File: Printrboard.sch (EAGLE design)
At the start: 121 parts, among them J1 MICROSD, J2 USB-MICROB, J3 ATX, Q1 RFP30N06LE, Q2 RFP30N06LE, Q3 RFP30N06LE, U1 LM2841, U2 A4982, U3 A4982, U4 A4982, U5 A4982, U6 AT90USB1286, U7 AP7313, U8 TXB0104, X1 16MHz

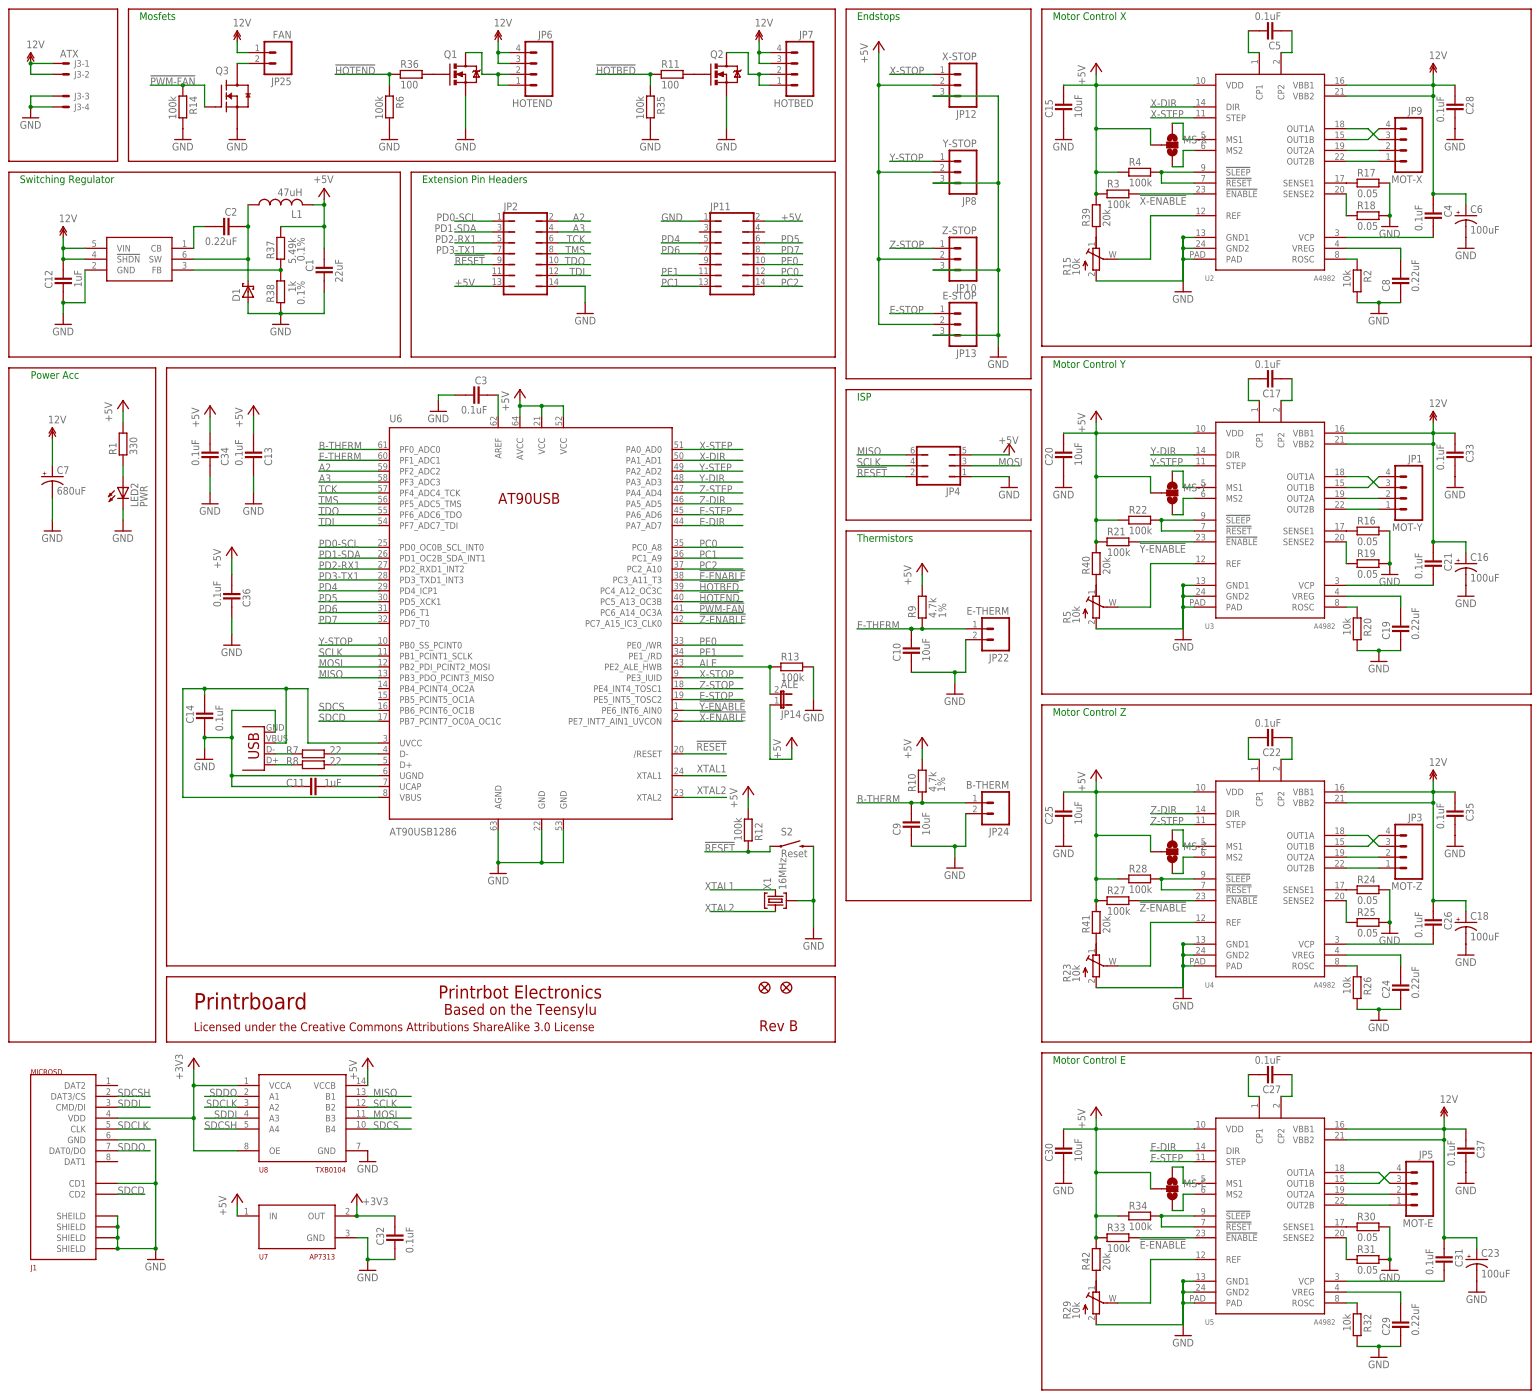
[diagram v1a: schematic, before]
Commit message: Change some caps around, add a solder jumper for USB sourced 5V, and modify silkscreen for production
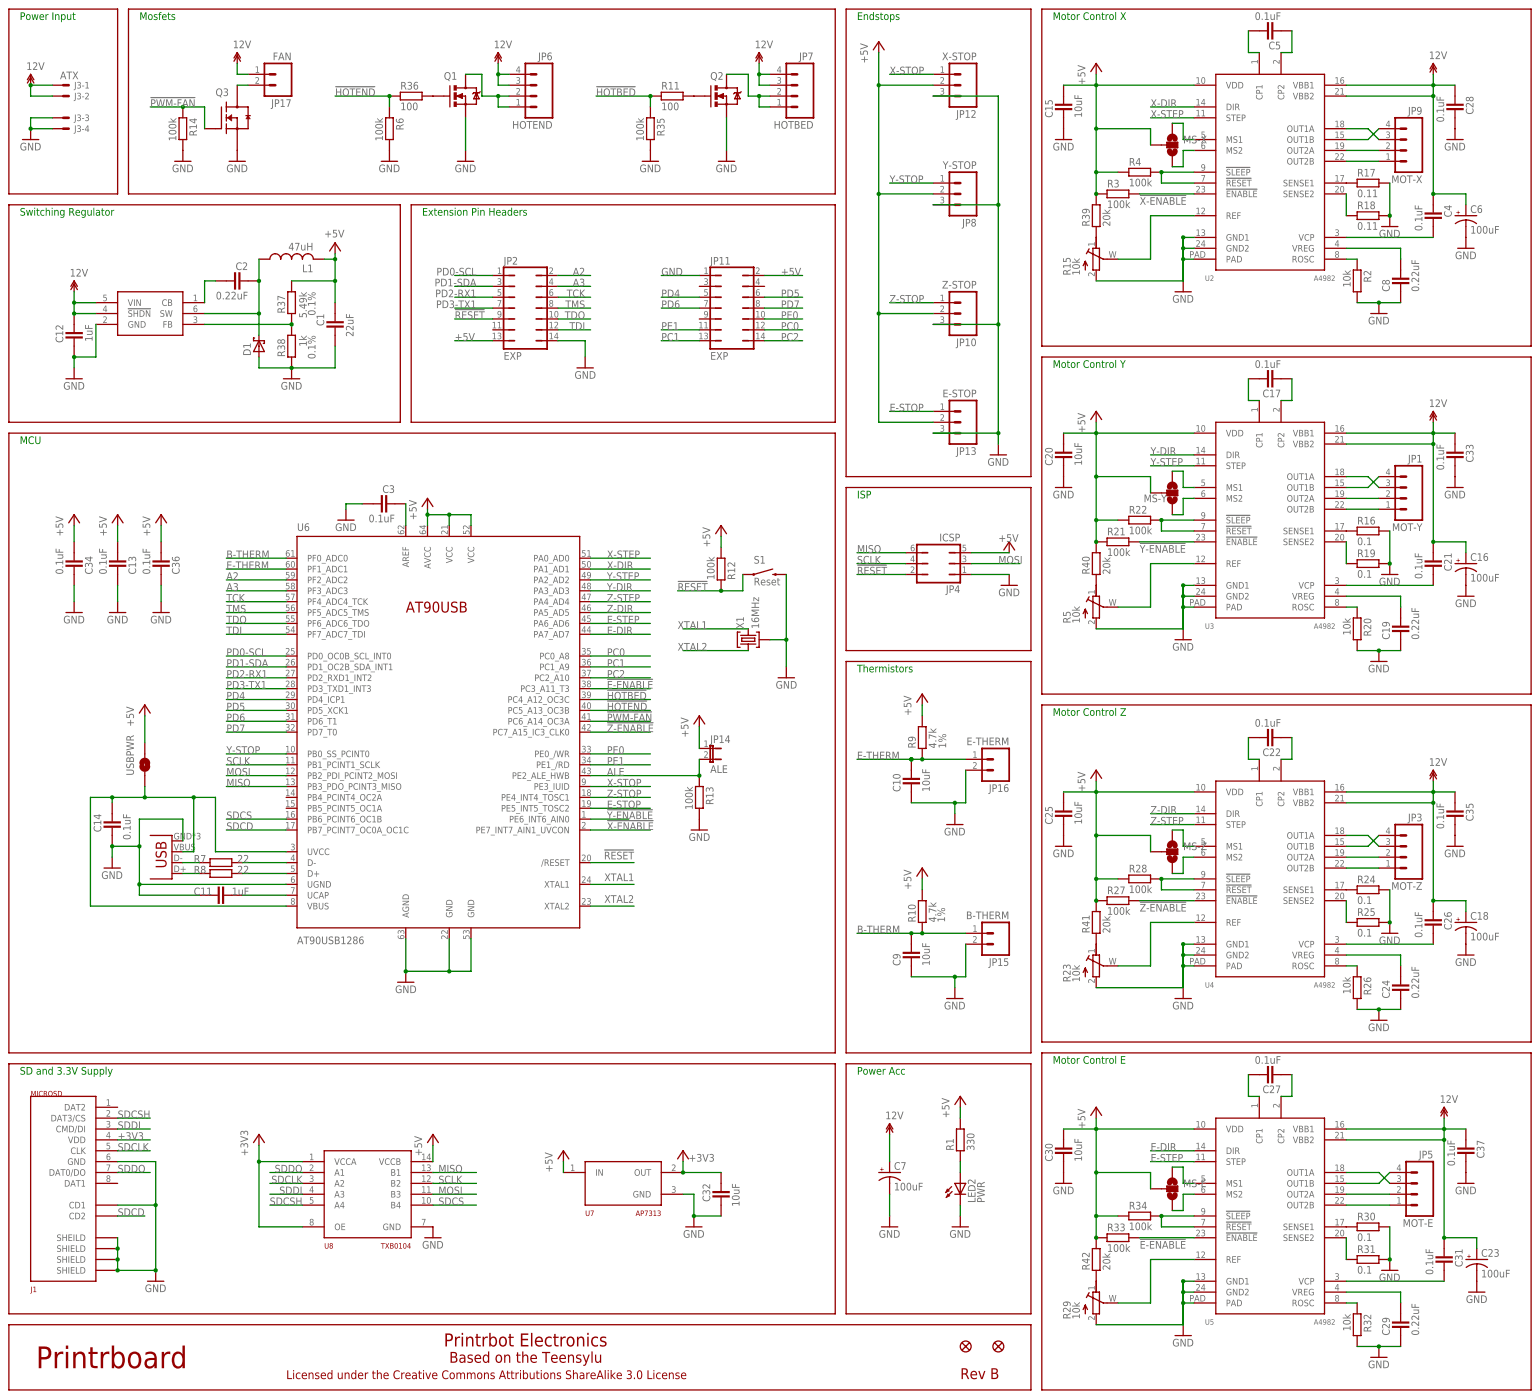
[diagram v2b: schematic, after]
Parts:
- removed J2: USB-MICROB, SparkFun:USB-MICROB
- removed JP22: E-THERM, SparkFun:M02PTH
- removed JP24: B-THERM, SparkFun:M02PTH
- removed JP25: FAN, SparkFun:M02PTH
- removed S2: Reset, SparkFun:SWITCH-MOMENTARY-2
- added JP15: B-THERM, SparkFun:M02PTH
- added JP16: E-THERM, SparkFun:M02PTH
- added JP17: FAN, SparkFun:M02PTH
- added S1: Reset, printrbot:SWITCH-MOMENTARY-2
- added USBPWR: SOLDERJUMPERNO, SparkFun:SOLDERJUMPERNO
- added X2: USB-MICROB, printrbot:USB-MICROB
- C32: value 0.1uF -> 10uF
- C7: value 680uF -> 100uF; device rcl:CPOL-USF -> rcl:CPOL-USD
- JP11, JP2: value (none) -> EXP
- JP4: value (none) -> ICSP
- R16, R19, R24, R25, R30, R31: value 0.05 -> 0.1
- R17, R18: value 0.05 -> 0.11
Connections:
- net !RESET: now also S1.1; no longer S2.1
- net +5V: now also USBPWR.2
- net 12V: now also JP17.1; no longer JP25.1
- net B-THERM: now also JP15.1; no longer JP24.1
- net E-THERM: now also JP16.1; no longer JP22.1
- net GND: now also JP15.2, JP16.2, S1.2, X2.GND; no longer J2.GND, JP22.2, JP24.2, S2.2
- net N$2: now also X2.D-; no longer J2.D-
- net N$5: now also X2.D+; no longer J2.D+
- net N$6: now also JP17.2; no longer JP25.2
- net VBUS: now also USBPWR.1, X2.VBUS; no longer J2.VBUS
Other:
- note added: "MCU"
- note added: "Power Input"
- note added: "SD and 3.3V Supply"
- moved on the sheet: C1, C10, C11, C12, C13, C14, C2, C3, C32, C34, C36, C7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

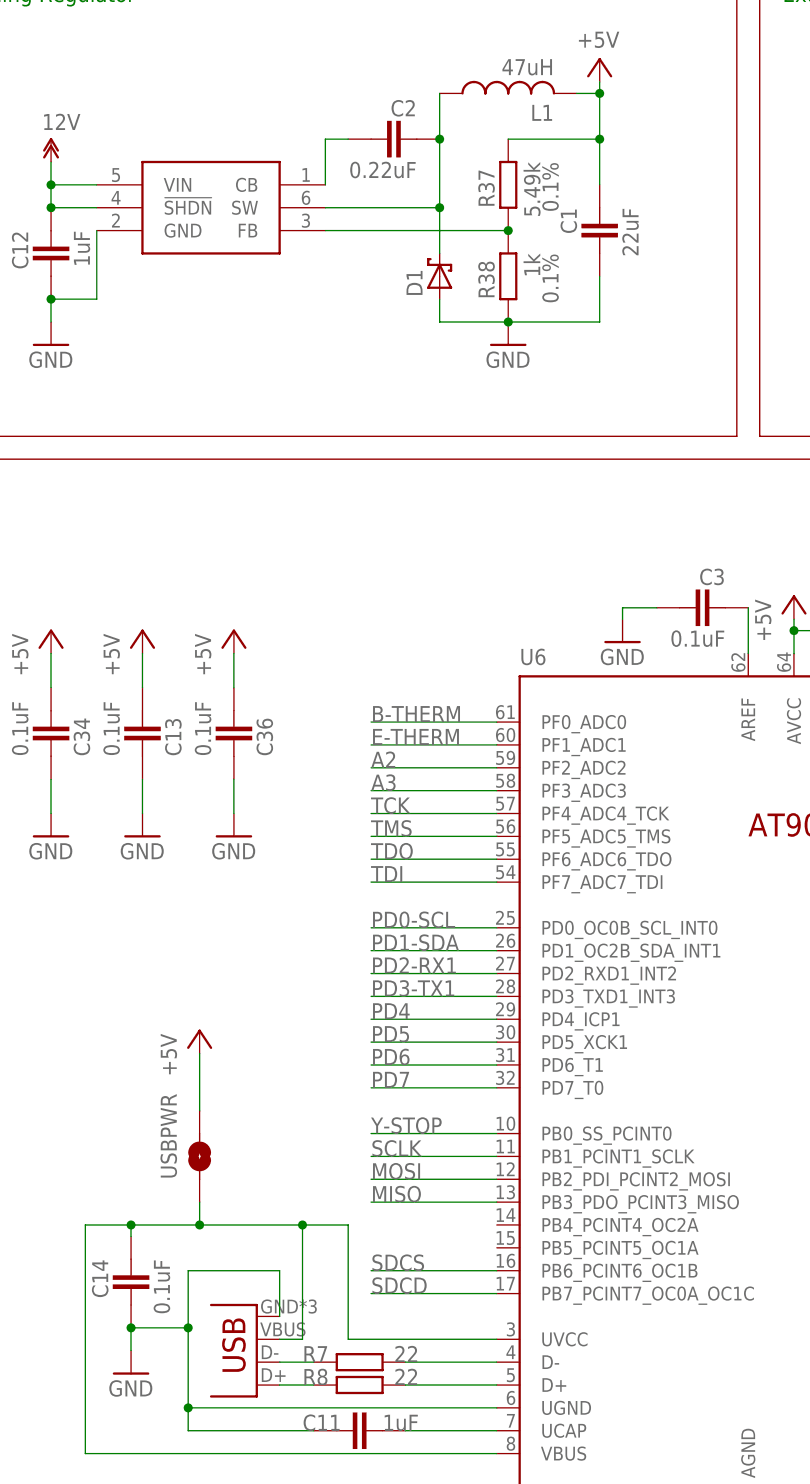
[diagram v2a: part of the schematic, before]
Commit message: Add extra solder pads for USB connector, and square up mounting holes
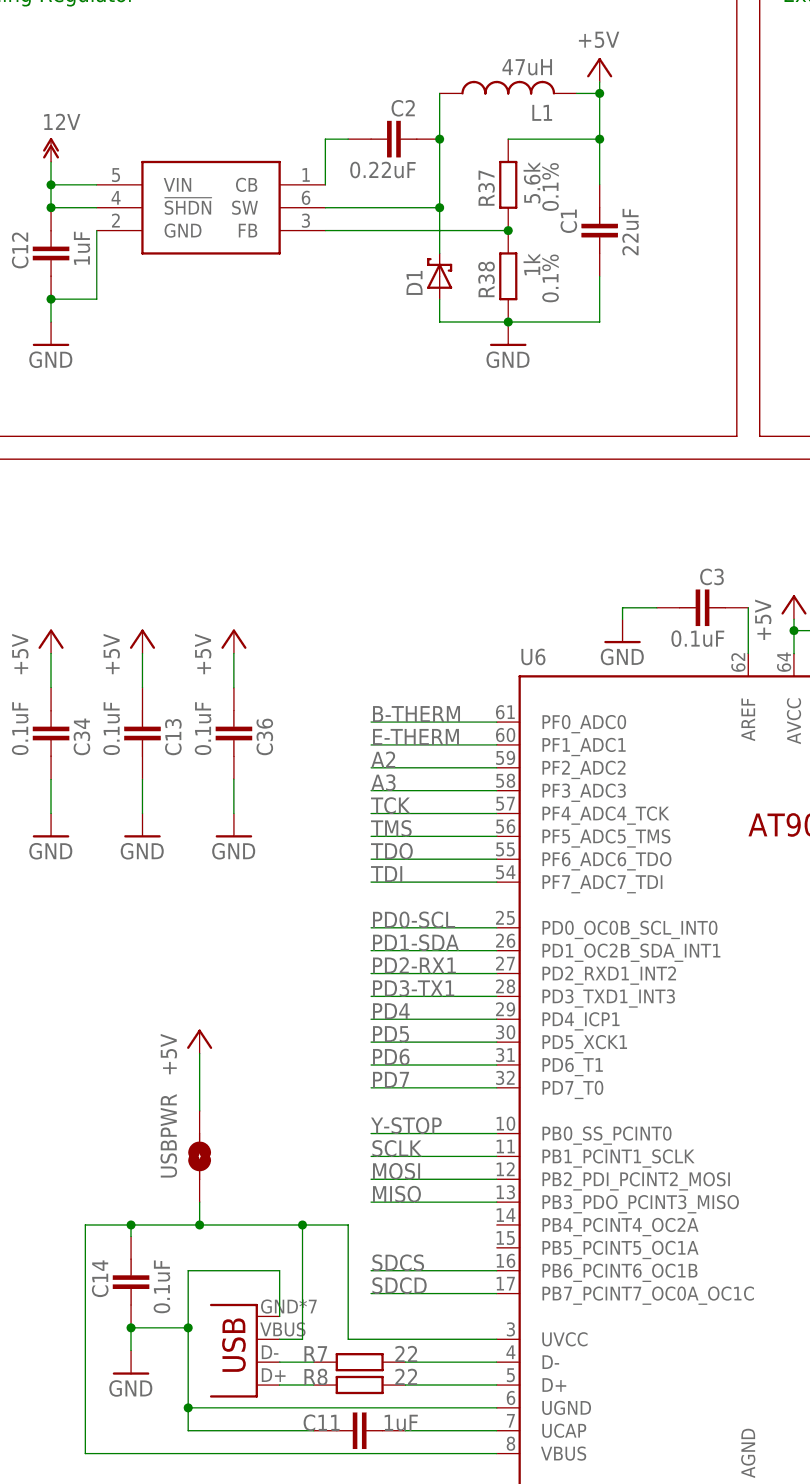
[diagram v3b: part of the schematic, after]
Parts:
- R37: value 5.49k -> 5.6k
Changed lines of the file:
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@@
 <?xml version="1.0" encoding="utf-8"?>
 <!DOCTYPE eagle SYSTEM "eagle.dtd">
-<eagle version="6.0">
+<eagle version="6.1">
 <drawing>
 <settings>
@@
 <setting verticaltext="up"/>
 </settings>
-<grid distance="0.1" unitdist="inch" unit="inch" style="lines" multiple="1" display="no" altdistance="0.05" altunitdist="inch" altunit="inch"/>
+<grid distance="0.1" unitdist="inch" unit="inch" style="lines" multiple="1" display="no" altdistance="0.01" altunitdist="inch" altunit="inch"/>
 <layers>
 <layer number="1" name="Top" color="4" fill="1" visible="no" active="no"/>
@@
 <part name="R36" library="ipc-7351-resistor" deviceset="RESISTOR_" device="0805" value="100"/>
 <part name="J1" library="printrbot" deviceset="MICROSD" device=""/>
-<part name="R37" library="ipc-7351-resistor" deviceset="RESISTOR_" device="0805" value="5.49k">
+<part name="R37" library="ipc-7351-resistor" deviceset="RESISTOR_" device="0805" value="5.6k">
 <attribute name="TOLERANCE" value="0.1%"/>
 </part>
